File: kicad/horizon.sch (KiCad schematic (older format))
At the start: 96 parts, among them J1 OLED, SW1 SW_Push, SW10 SW_Push, SW11 SW_Push, SW12 SW_Push, SW13 SW_Push, SW14 SW_Push, SW15 SW_Push, SW16 SW_Push, SW17 SW_Push, SW18 SW_Push, SW19 SW_Push, SW2 SW_Push, SW20 SW_Push, SW21 SW_Push, SW22 SW_Push, SW23 SW_Push, SW24 SW_Push, SW25 SW_Push, SW26 SW_Push, SW27 SW_Push, SW28 SW_Push, SW29 SW_Push, SW3 SW_Push, SW30 SW_Push, SW31 SW_Push, SW32 SW_Push, SW33 SW_Push, SW34 SW_Push, SW35 SW_Push, SW36 SW_Push, SW37 SW_Push, SW38 SW_Push, SW39 SW_Push, SW4 SW_Push, SW40 SW_Push, SW41 SW_Push, SW42 SW_Push, SW5 SW_Push, SW6 SW_Push, SW7 SW_Push, SW8 SW_Push, SW9 SW_Push, U1 PRO-MICRO

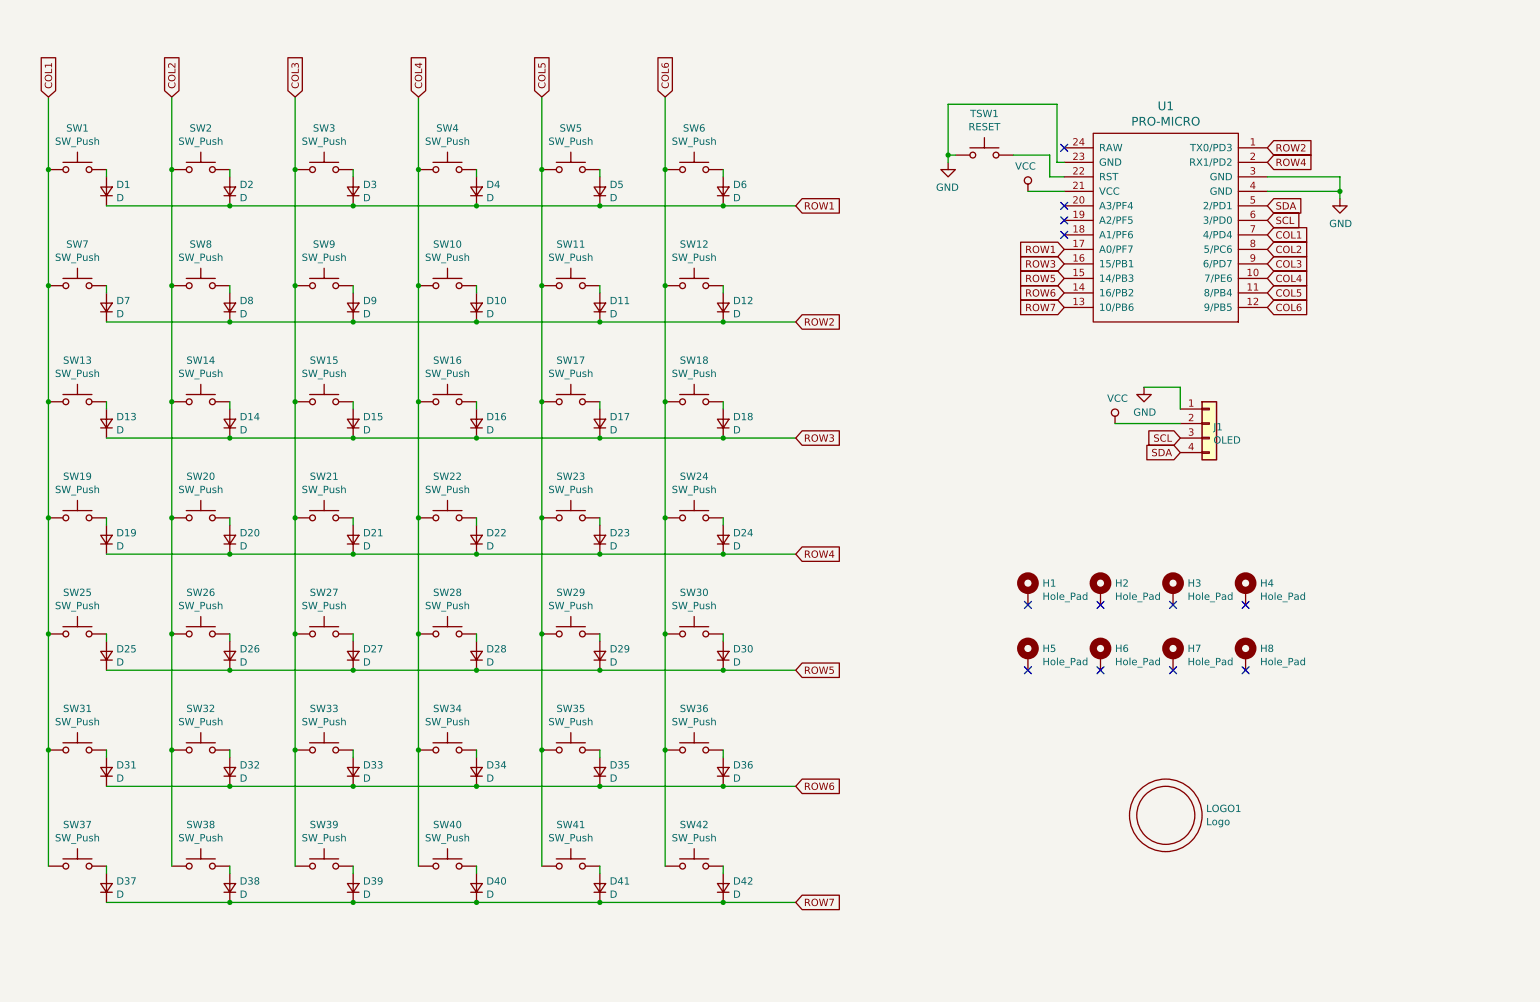
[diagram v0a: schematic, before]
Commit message: Use 50 key layout on MX version
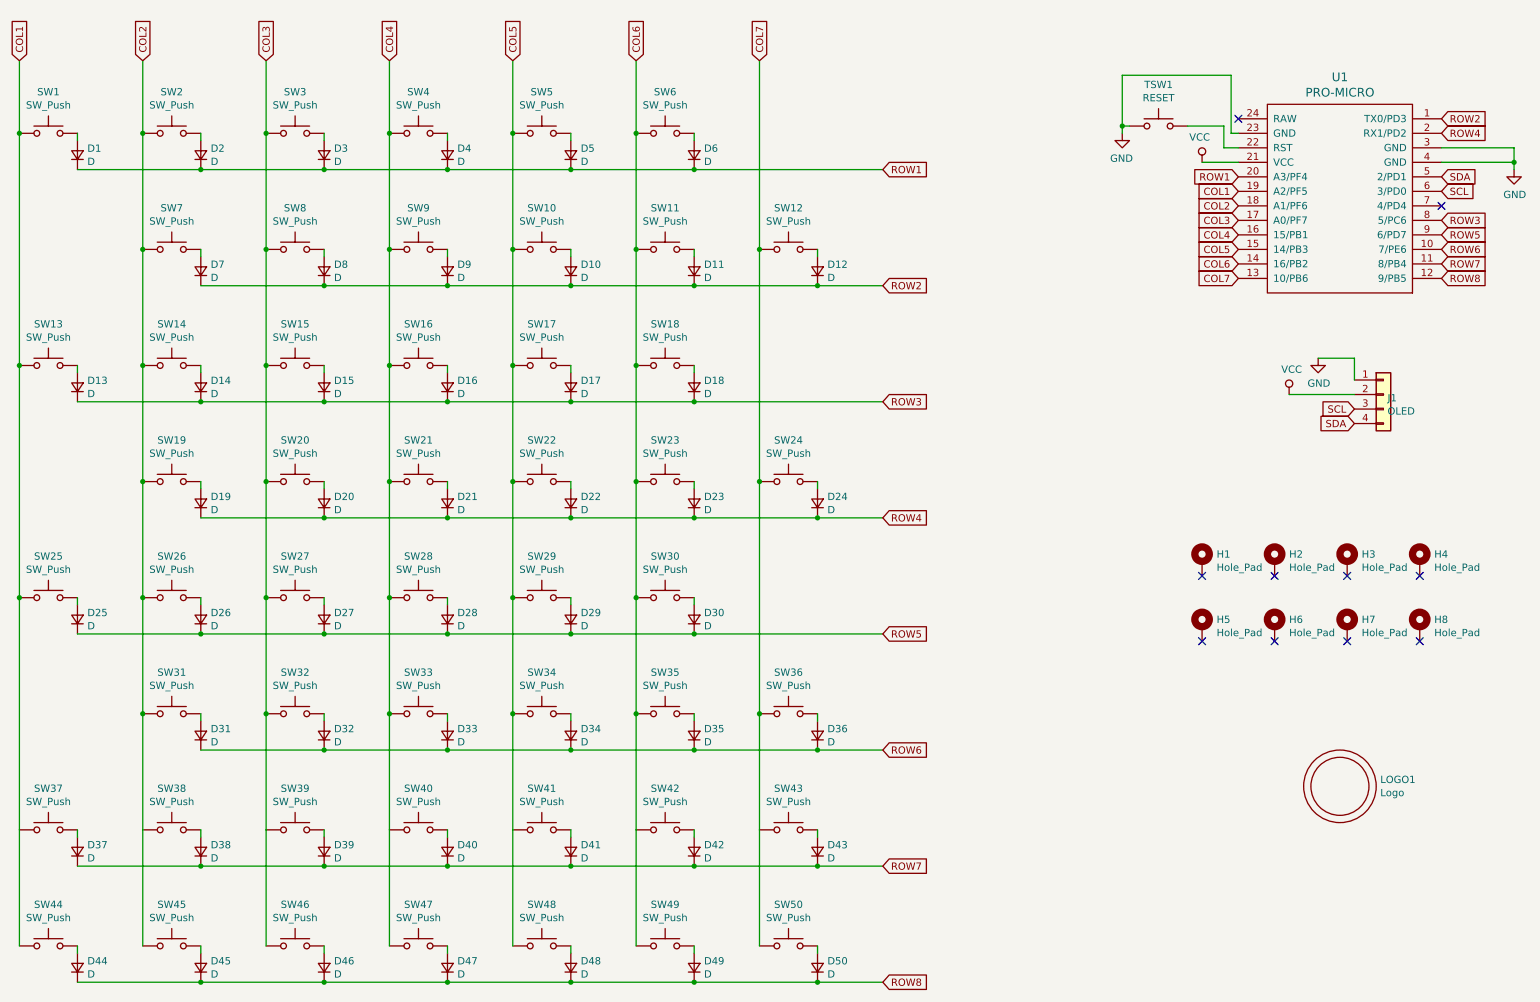
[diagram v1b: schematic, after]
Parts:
- removed D1, D13, D19, D20, D25, D31, D32, D37, D7, D8: D, horizon-footprints:D_SOD-123, symbol horizon-components:D
- removed SW1, SW13, SW19, SW20, SW25, SW31, SW32, SW37, SW7, SW8: SW_Push, horizon-footprints:SW_MX, symbol horizon-components:SW_Push
- added D11, D12, D18, D23, D24, D30, D35, D36, D42, D43, D44, D45, D46, D47, D48, D49, D50, D6: D, horizon-footprints:D_SOD-123, symbol horizon-components:D
- added SW11, SW12, SW18, SW23, SW24, SW30, SW35, SW36, SW42, SW43, SW44, SW45, SW46, SW47, SW48, SW49, SW50, SW6: SW_Push, horizon-footprints:SW_MX, symbol horizon-components:SW_Push
- renumbered D2 to D1, D12 to D10, D14 to D13, D15 to D14, D16 to D15, D17 to D16, D18 to D17, D21 to D19, D3 to D2, D22 to D20, D23 to D21, D24 to D22, D26 to D25, D27 to D26, D28 to D27, D29 to D28, D30 to D29, D4 to D3, D33 to D31, D34 to D32, D35 to D33, D36 to D34, D38 to D37, D39 to D38, D40 to D39, D5 to D4, D41 to D40, D42 to D41, D6 to D5, D9 to D7, D10 to D8, D11 to D9, SW2 to SW1, SW12 to SW10, SW14 to SW13, SW15 to SW14, SW16 to SW15, SW17 to SW16, SW18 to SW17, SW21 to SW19, SW3 to SW2, SW22 to SW20, SW23 to SW21, SW24 to SW22, SW26 to SW25, SW27 to SW26, SW28 to SW27, SW29 to SW28, SW30 to SW29, SW4 to SW3, SW33 to SW31, SW34 to SW32, SW35 to SW33, SW36 to SW34, SW38 to SW37, SW39 to SW38, SW40 to SW39, SW5 to SW4, SW41 to SW40, SW42 to SW41, SW6 to SW5, SW9 to SW7, SW10 to SW8, SW11 to SW9
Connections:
- net COL1: now also SW1.1, SW13.1, SW25.1, SW37.1, U1.19 (A2/PF5), SW44.1; no longer U1.7 (4/PD4)
- net COL2: now also SW14.1, SW19.1, SW2.1, SW26.1, SW31.1, SW38.1, SW7.1, U1.18 (A1/PF6), SW45.1; no longer SW1.1, SW13.1, SW25.1, SW37.1, U1.8 (5/PC6)
- net COL3: now also SW15.1, SW20.1, SW27.1, SW3.1, SW32.1, SW39.1, SW8.1, U1.17 (A0/PF7), SW46.1; no longer SW14.1, SW19.1, SW2.1, SW26.1, SW31.1, SW38.1, SW7.1, U1.9 (6/PD7)
- net COL4: now also SW16.1, SW21.1, SW28.1, SW33.1, SW4.1, SW40.1, SW9.1, U1.16 (15/PB1), SW47.1; no longer SW15.1, SW20.1, SW27.1, SW3.1, SW32.1, SW39.1, SW8.1, U1.10 (7/PE6)
- net COL5: now also SW10.1, SW17.1, SW22.1, SW29.1, SW34.1, SW41.1, SW5.1, U1.15 (14/PB3), SW48.1; no longer SW16.1, SW21.1, SW28.1, SW33.1, SW4.1, SW40.1, SW9.1, U1.11 (8/PB4)
- net COL6: now also U1.14 (16/PB2), SW11.1, SW18.1, SW23.1, SW30.1, SW35.1, SW42.1, SW49.1, SW6.1; no longer SW10.1, SW17.1, SW22.1, SW29.1, SW34.1, SW41.1, SW5.1, U1.12 (9/PB5)
- net ROW1: now also U1.20 (A3/PF4), D6.1 (K); no longer U1.17 (A0/PF7)
- net ROW2: now also D11.1 (K), D12.1 (K)
- net ROW3: now also U1.8 (5/PC6), D18.1 (K); no longer U1.16 (15/PB1)
- net ROW4: now also D23.1 (K), D24.1 (K)
- net ROW5: now also U1.9 (6/PD7), D30.1 (K); no longer U1.15 (14/PB3)
- net ROW6: now also U1.10 (7/PE6), D35.1 (K), D36.1 (K); no longer U1.14 (16/PB2)
- net ROW7: now also U1.11 (8/PB4), D42.1 (K), D43.1 (K); no longer U1.13 (10/PB6)
- new net: D42.2 (A), SW42.2
- new net: D43.2 (A), SW43.2
- new net: D30.2 (A), SW30.2
- new net: D18.2 (A), SW18.2
- new net: D6.2 (A), SW6.2
- new net: D35.2 (A), SW35.2
- new net: D36.2 (A), SW36.2
- new net: D23.2 (A), SW23.2
- new net: D24.2 (A), SW24.2
- new net: D11.2 (A), SW11.2
- new net: D12.2 (A), SW12.2
- new net: D47.2 (A), SW47.2
- new net: D48.2 (A), SW48.2
- new net: D45.2 (A), SW45.2
- new net: D46.2 (A), SW46.2
- new net: D44.2 (A), SW44.2
- new net: D49.2 (A), SW49.2
- new net: D50.2 (A), SW50.2
- new net COL7: SW12.1, SW24.1, SW36.1, SW43.1, SW50.1, U1.13 (10/PB6)
- new net ROW8: D44.1 (K), D45.1 (K), D46.1 (K), D47.1 (K), D48.1 (K), D49.1 (K), D50.1 (K), U1.12 (9/PB5)
- no-connect marks 12 -> 10
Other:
- moved on the sheet: D1, D10, D13, D14, D15, D16, D17, D19, D2, D20, D21, D22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

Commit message: Clean up MX version before overhaul
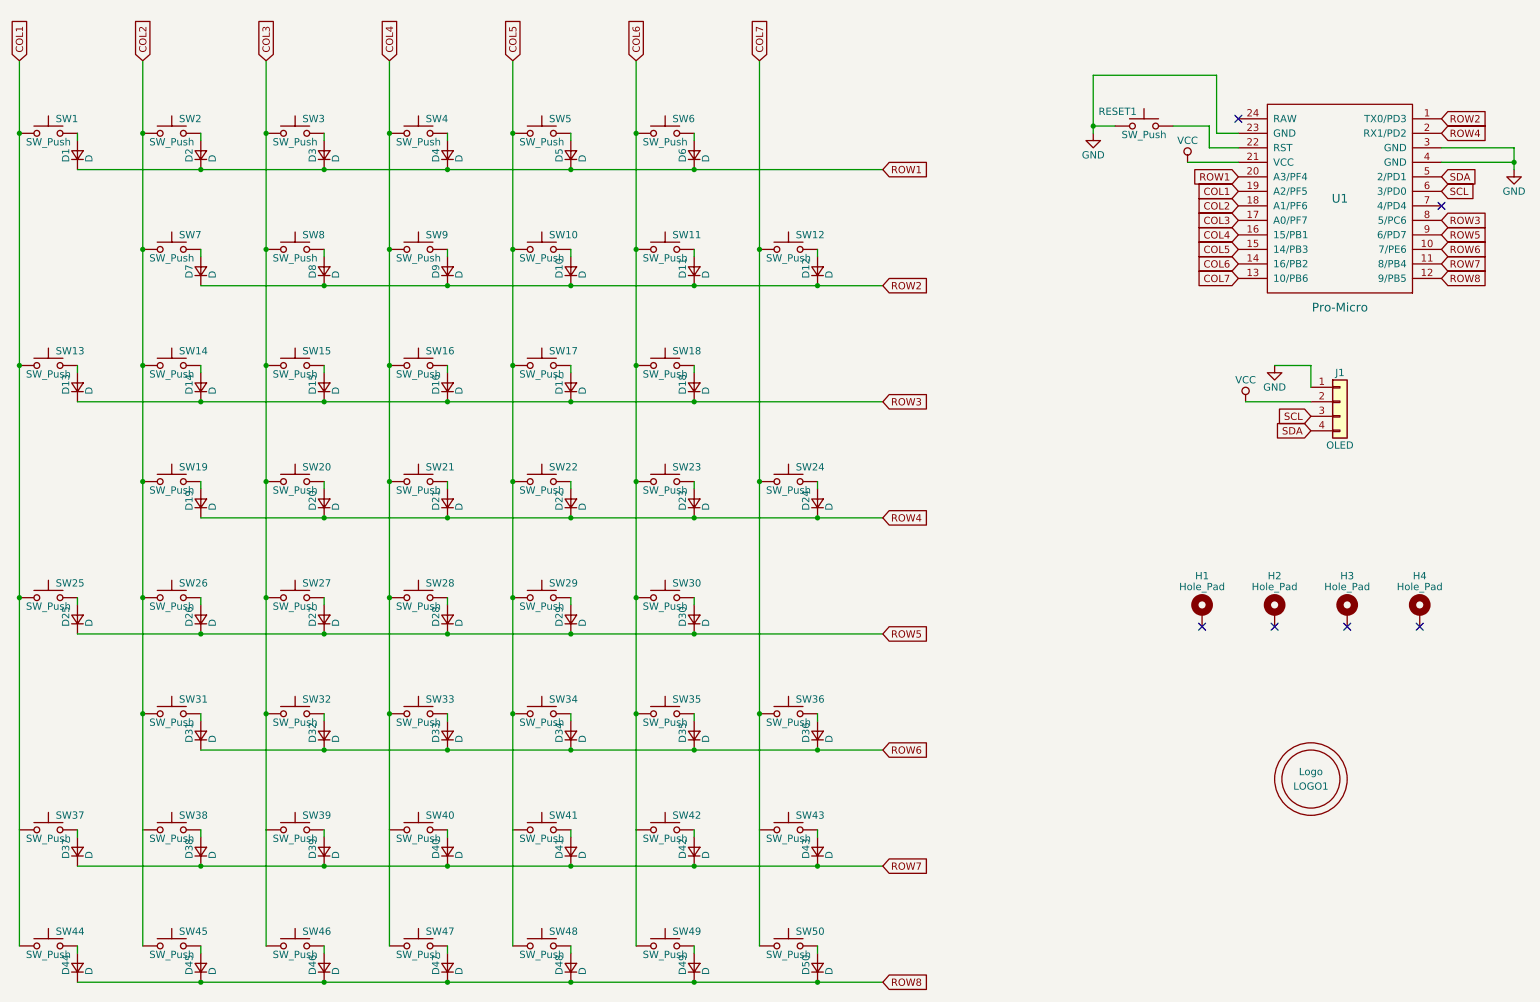
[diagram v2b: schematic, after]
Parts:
- removed H5, H6, H7, H8: Hole_Pad, horizon-footprints:Mount_M2, symbol horizon-components:Hole_Pad
- RESET1: renamed from TSW1; value RESET -> SW_Push
- U1: value PRO-MICRO -> Pro-Micro
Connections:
- no-connect marks 10 -> 6
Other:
- moved on the sheet: H1, H2, H3, H4, J1, LOGO1, RESET1

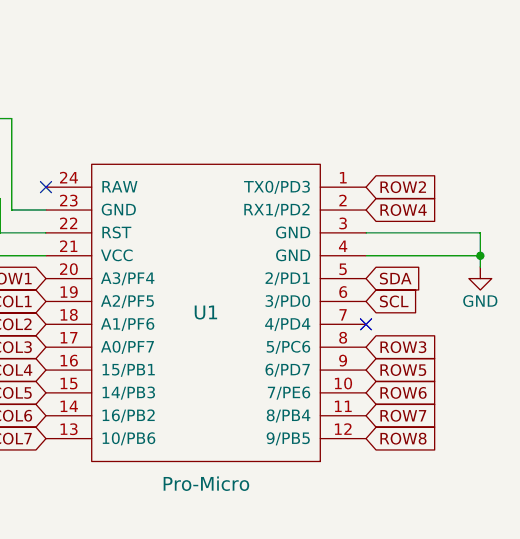
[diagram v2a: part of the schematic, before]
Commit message: Implement battery on Choc version, plus bottom and top PCBs
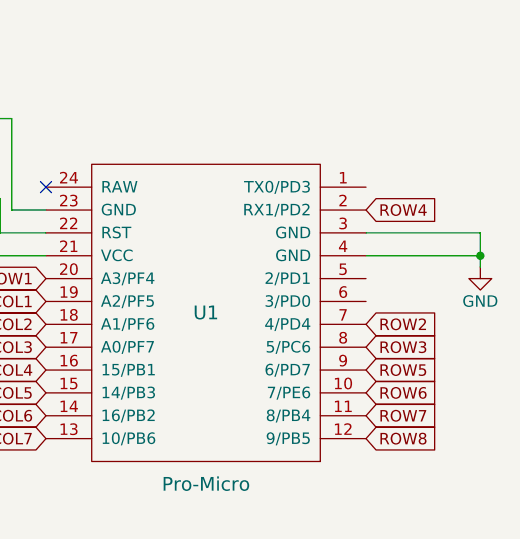
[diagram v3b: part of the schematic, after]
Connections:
- net ROW2: now also U1.7 (4/PD4); no longer U1.1 (TX0/PD3)
- net SCL: no longer U1.6 (3/PD0)
- net SDA: no longer U1.5 (2/PD1)
- no-connect marks 6 -> 5
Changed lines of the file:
@@
 Text GLabel 6550 5550 2    50   Input ~ 0
 ROW6
-Text GLabel 10400 1200 2    50   Input ~ 0
+Text GLabel 10400 1800 2    50   Input ~ 0
 ROW2
 Text GLabel 10400 2200 2    50   Input ~ 0
@@
 Text GLabel 10400 2300 2    50   Input ~ 0
 ROW8
-NoConn ~ 10400 1800
 Text GLabel 9000 1800 0    50   Input ~ 0
 COL2
@@
 	1    0    0    -1
 $EndComp
-Text GLabel 10400 1600 2    50   Input ~ 0
-SDA
-Text GLabel 10400 1700 2    50   Input ~ 0
-SCL
 NoConn ~ 9000 1200
 $EndSCHEMATC

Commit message: Layout MX PCB
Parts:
- removed J1: OLED, horizon-footprints:Header_1x04_2.54mm, symbol horizon-components:Conn_01x04
- added D51, D52: D, horizon-footprints:D_SOD-123, symbol horizon-components:D
- added H5, H6, H7, H8: Hole_Pad, horizon-footprints:Mount_M2, symbol horizon-components:Hole_Pad
- added SS1: POWER, horizon-footprints:SS12D00, symbol horizon-components:SW_SPDT
- added SW51, SW52: SW_Push, horizon-footprints:SW_MX, symbol horizon-components:SW_Push
- added TB1: BATTERY, horizon-footprints:KF350-2P, symbol horizon-components:Conn_01x02
- BTN1: renamed from RESET1; value SW_Push -> RESET
- LOGO1: footprint horizon-footprints:Logo_Horizon -> horizon-footprints:Logo_Horizon_Small
- U1: value Pro-Micro -> PRO-MICRO
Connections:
- net COL1: now also SW39.1; no longer SW37.1, SW44.1
- net COL2: now also SW40.1; no longer SW19.1, SW31.1, SW38.1, SW45.1, SW7.1
- net COL3: now also SW41.1; no longer SW20.1, SW32.1, SW39.1, SW46.1, SW8.1
- net COL4: now also SW42.1; no longer SW21.1, SW33.1, SW40.1, SW47.1, SW9.1
- net COL5: now also SW43.1; no longer SW10.1, SW22.1, SW34.1, SW41.1, SW48.1
- net COL6: now also SW44.1; no longer SW11.1, SW23.1, SW35.1, SW42.1, SW49.1
- net COL7: now also SW31.1, SW45.1; no longer SW12.1, SW24.1, SW36.1, SW43.1, SW50.1
- net GND: now also TB1.1 (Pin_1)
- net ROW1: now also D10.1 (K), D11.1 (K), D12.1 (K), D7.1 (K), D8.1 (K), D9.1 (K), U1.1 (TX0/PD3); no longer U1.20 (A3/PF4)
- net ROW2: now also D13.1 (K), D14.1 (K), D15.1 (K), D16.1 (K), D17.1 (K), D18.1 (K), D19.1 (K), D20.1 (K), D21.1 (K), D22.1 (K), D23.1 (K), D24.1 (K), U1.2 (RX1/PD2); no longer D10.1 (K), D11.1 (K), D12.1 (K), D7.1 (K), D8.1 (K), D9.1 (K), U1.7 (4/PD4)
- net ROW3: now also D25.1 (K), D26.1 (K), D27.1 (K), D28.1 (K), D29.1 (K), D30.1 (K), D31.1 (K), D32.1 (K), D33.1 (K), D34.1 (K), D35.1 (K), D36.1 (K), D37.1 (K), D38.1 (K), U1.5 (2/PD1); no longer D13.1 (K), D14.1 (K), D15.1 (K), D16.1 (K), D17.1 (K), D18.1 (K), U1.8 (5/PC6)
- net ROW4: now also D39.1 (K), D40.1 (K), D41.1 (K), D42.1 (K), D43.1 (K), D44.1 (K), D45.1 (K), D46.1 (K), D47.1 (K), D48.1 (K), D49.1 (K), D50.1 (K), U1.20 (A3/PF4), D51.1 (K), D52.1 (K); no longer D19.1 (K), D20.1 (K), D21.1 (K), D22.1 (K), D23.1 (K), D24.1 (K), U1.2 (RX1/PD2)
- net RESET: now reaches BTN1.1, U1.22 (RST)
- net RAW: now reaches U1.24 (RAW)
- net RAW: now also SS1.3 (C)
- net COL14: now reaches U1.6 (3/PD0)
- net COL14: now also SW12.1, SW24.1, SW38.1, SW52.1
- removed net ROW5: D25.1 (K), D26.1 (K), D27.1 (K), D28.1 (K), D29.1 (K), D30.1 (K), U1.9 (6/PD7)
- removed net ROW6: D31.1 (K), D32.1 (K), D33.1 (K), D34.1 (K), D35.1 (K), D36.1 (K), U1.10 (7/PE6)
- removed net ROW7: D37.1 (K), D38.1 (K), D39.1 (K), D40.1 (K), D41.1 (K), D42.1 (K), D43.1 (K), U1.11 (8/PB4)
- removed net ROW8: D44.1 (K), D45.1 (K), D46.1 (K), D47.1 (K), D48.1 (K), D49.1 (K), D50.1 (K), U1.12 (9/PB5)
- new net: D51.2 (A), SW51.2
- new net: D52.2 (A), SW52.2
- new net +BATT: SS1.2 (B), TB1.2 (Pin_2)
- new net COL10: SW20.1, SW34.1, SW48.1, SW8.1, U1.10 (7/PE6)
- new net COL11: SW21.1, SW35.1, SW49.1, SW9.1, U1.9 (6/PD7)
- new net COL12: SW10.1, SW22.1, SW36.1, SW50.1, U1.8 (5/PC6)
- new net COL13: SW11.1, SW23.1, SW37.1, SW51.1, U1.7 (4/PD4)
- new net COL8: SW32.1, SW46.1, U1.12 (9/PB5)
- new net COL9: SW19.1, SW33.1, SW47.1, SW7.1, U1.11 (8/PB4)
- no-connect marks 5 -> 9
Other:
- moved on the sheet: BTN1, H1, H2, H3, H4, LOGO1, U1
